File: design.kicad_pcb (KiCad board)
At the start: 2 copper layers, 20 x 10 mm, 11 parts, among them J1 Conn_01x03_Female

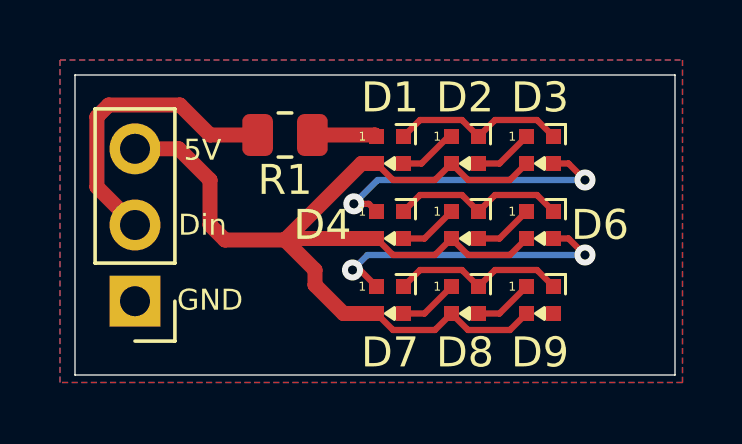
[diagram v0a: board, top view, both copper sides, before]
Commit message: PCB cleanup
no functional changes.
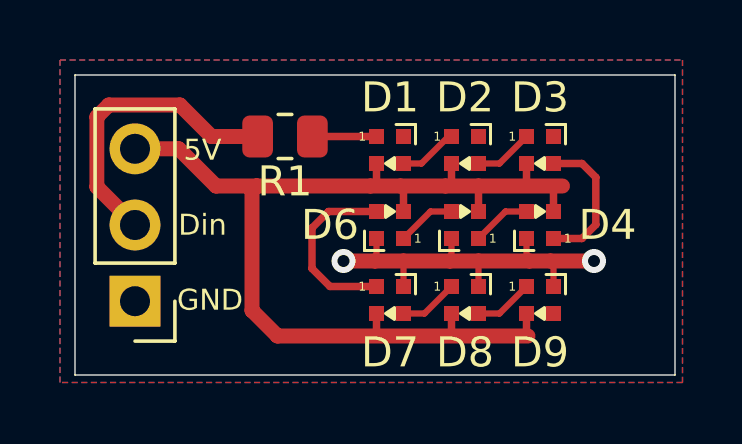
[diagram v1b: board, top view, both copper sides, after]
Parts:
- moved D4 5.00 mm to (161.5, 97.0), turned to 180 degrees
- moved D6 5.00 mm to (156.5, 97.0), turned to 180 degrees
- turned D5 to 180 degrees
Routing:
- net Net-(D3-Pad3): track 10.2 -> 4.79 mm, vias 2 -> 0
- net GND: track 17.7 -> 13.3 mm, vias 0 -> 2
- net Net-(D6-Pad3): track 10.3 -> 6.13 mm, vias 2 -> 0
- net VCC: track 36.4 -> 34.1 mm

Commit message: add more GND vias
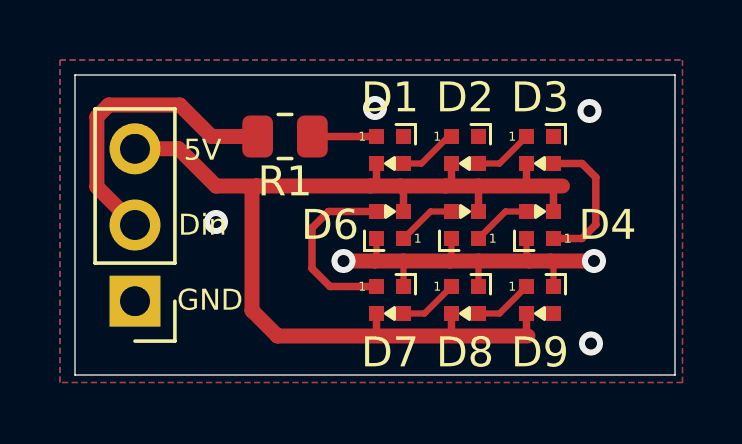
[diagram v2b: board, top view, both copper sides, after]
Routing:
- net GND: vias 2 -> 6
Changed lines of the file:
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@@
   (segment (start 156 98.2) (end 154.95 98.2) (width 0.5) (layer "F.Cu") (net 4))
   (via (at 163.3 98.2) (size 0.8) (drill 0.4) (layers "F.Cu" "B.Cu") (net 4))
+  (via (at 163.15 93.2) (size 0.8) (drill 0.4) (layers "F.Cu" "B.Cu") (free) (net 4))
+  (via (at 156 93.1) (size 0.8) (drill 0.4) (layers "F.Cu" "B.Cu") (free) (net 4))
+  (via (at 163.2 100.95) (size 0.8) (drill 0.4) (layers "F.Cu" "B.Cu") (free) (net 4))
   (via (at 154.95 98.2) (size 0.8) (drill 0.4) (layers "F.Cu" "B.Cu") (net 4))
+  (via (at 150.7 96.9) (size 0.8) (drill 0.4) (layers "F.Cu" "B.Cu") (free) (net 4))
   (segment (start 160.15 94.95) (end 161.05 94.05) (width 0.21) (layer "F.Cu") (net 5))
   (segment (start 159.45 94.95) (end 160.15 94.95) (width 0.21) (layer "F.Cu") (net 5))
